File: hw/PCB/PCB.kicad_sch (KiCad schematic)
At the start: 283 parts, among them IC1 TXU0101DCKR, IC2 W25Q64JVXGIQ_TR, J1 USB_C_Receptacle_USB2.0, J2 Adafruit TFT, J3 Conn_ARM_JTAG_SWD_10, J4 Conn_01x03_Pin, K1 KEYSW, K10 KEYSW, K11 KEYSW, K12 KEYSW, K13 KEYSW, K14 KEYSW, K15 KEYSW, K16 KEYSW, K17 KEYSW, K18 KEYSW, K19 KEYSW, K2 KEYSW, K20 KEYSW, K21 KEYSW, K22 KEYSW, K23 KEYSW, K24 KEYSW, K25 KEYSW, K26 KEYSW, K27 KEYSW, K28 KEYSW, K29 KEYSW, K3 KEYSW, K31 KEYSW, K32 KEYSW, K33 KEYSW, K34 KEYSW, K35 KEYSW, K36 KEYSW, K37 KEYSW, K38 KEYSW, K39 KEYSW, K4 KEYSW, K40 KEYSW, K41 KEYSW, K42 KEYSW, K43 KEYSW, K46 KEYSW, K47 KEYSW, K48 KEYSW, K49 KEYSW, K5 KEYSW, K50 KEYSW, K51 KEYSW, K52 KEYSW, K53 KEYSW, K54 KEYSW, K55 KEYSW, K56 KEYSW, K57 KEYSW, K58 KEYSW, K59 KEYSW, K6 KEYSW, K61 KEYSW, K62 KEYSW, K63 KEYSW, K64 KEYSW, K65 KEYSW, K66 KEYSW, K67 KEYSW, K68 KEYSW, K69 KEYSW, K7 KEYSW, K8 KEYSW, K9 KEYSW, SW2 RotaryEncoder_Switch, U2 nRF52840-MS88SF2, U3 74HC595, U4 74HC595, U5 nPM1300-QEAA

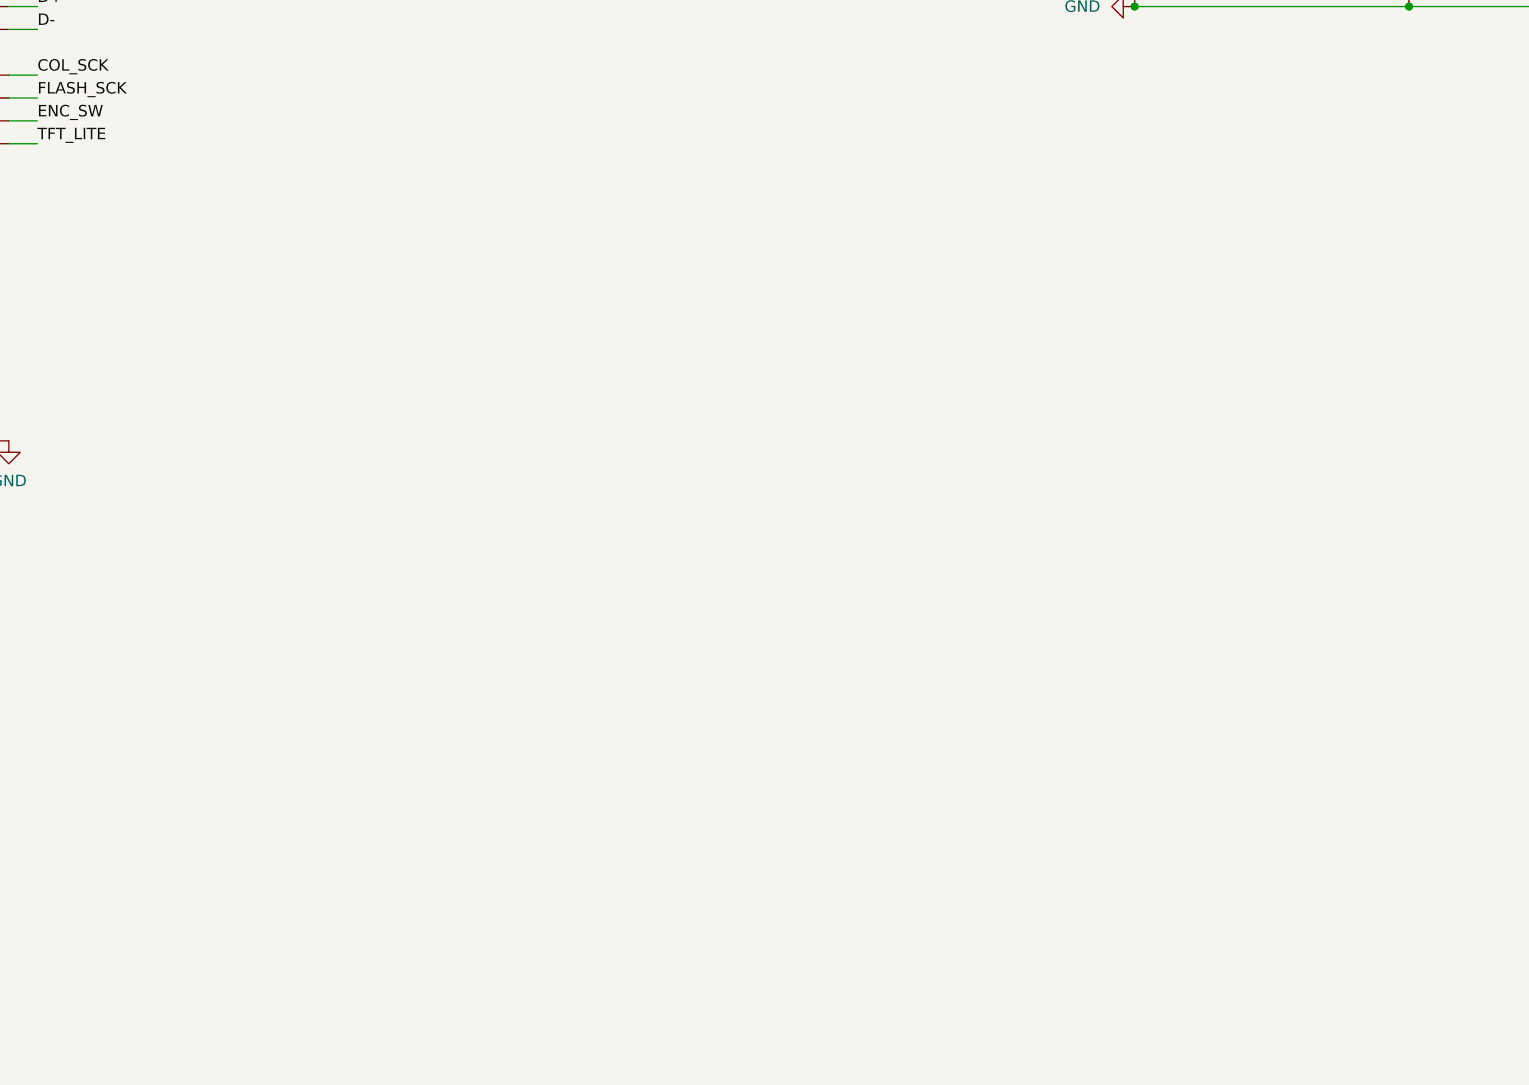
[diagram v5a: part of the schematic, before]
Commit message: Added XIAO and ItsyBitsy
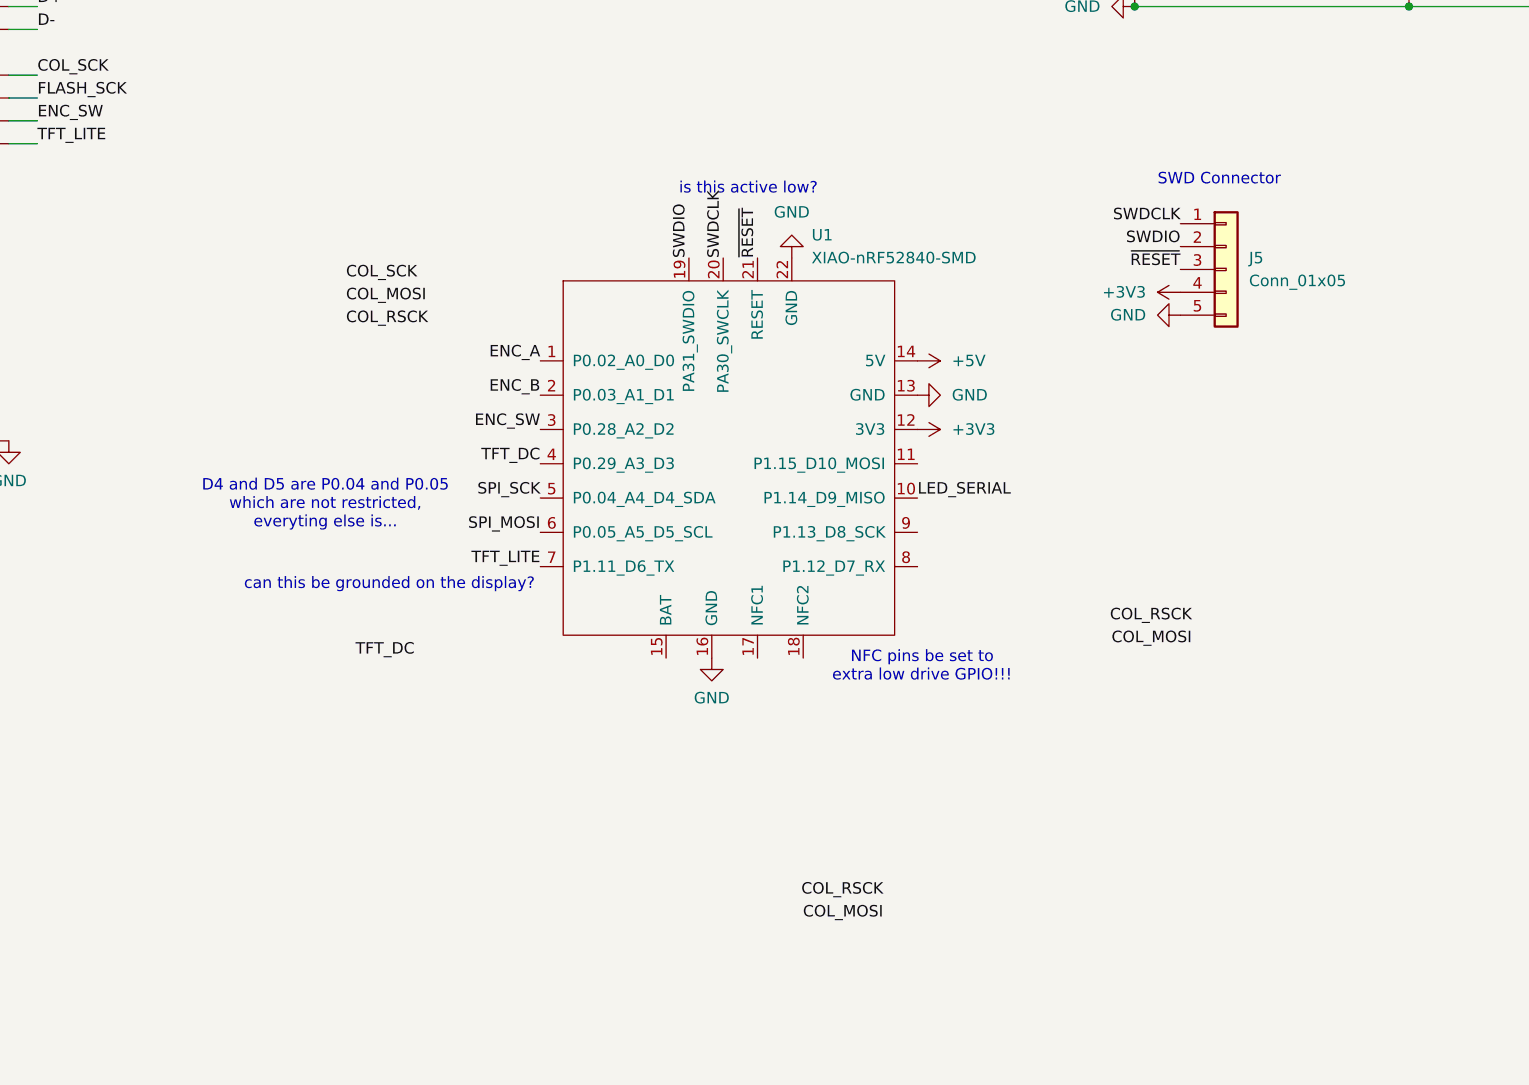
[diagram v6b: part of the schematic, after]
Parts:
- added J5: Conn_01x05, symbol Connector_Generic:Conn_01x05
- added U1: XIAO-nRF52840-SMD, Seeed Studio XIAO Series Library:XIAO-nRF52840-SMD, symbol Seeed_Studio_XIAO_Series:XIAO-nRF52840-SMD
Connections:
- net ENC_A: now also U1.1 (P0.02_A0_D0)
- net ENC_B: now also U1.2 (P0.03_A1_D1)
- net ENC_SW: now also U1.3 (P0.28_A2_D2)
- net GND: now also J5.5 (Pin_5), U1.13 (GND), U1.16 (GND), U1.22 (GND)
- net LED_SERIAL: now also U1.10 (P1.14_D9_MISO)
- net SWDCLK: now also J5.1 (Pin_1), U1.20 (PA30_SWCLK)
- net SWDIO: now also J5.2 (Pin_2), U1.19 (PA31_SWDIO)
- net TFT_DC: now also U1.4 (P0.29_A3_D3)
- net TFT_LITE: now also U1.7 (P1.11_D6_TX)
- net ~{RESET}: now also J5.3 (Pin_3), U1.21 (RESET)
- new net +3V3: J5.4 (Pin_4), U1.12 (3V3)
- new net +5V: U1.14 (5V)
- new net SPI_MOSI: U1.6 (P0.05_A5_D5_SCL)
- new net SPI_SCK: U1.5 (P0.04_A4_D4_SDA)
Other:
- note added: "D4 and D5 are P0.04 and P0.05 which are not restricted, everyting else is..."
- note added: "NFC pins be set to extra low drive GPIO!!!"
- note added: "SWD Connector"
- note added: "can this be grounded on the display?"
- note added: "is this active low?"

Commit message: beep boop more changes
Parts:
- removed BT1: ~, Connector_JST:JST_GH_SM03B-GHS-TB_1x03-1MP_P1.25mm_Horizontal, symbol PCB-altium-import:root_0_Battery_pack_NTC
- removed C11: 2.2uF, Capacitor_SMD:C_0603_1608Metric, symbol Device:C
- removed C12: 100nF, Capacitor_SMD:C_0201_0603Metric, symbol Device:C
- removed C13, C93: 1uF, Capacitor_SMD:C_0603_1608Metric, symbol Device:C
- removed C16: 10uF, Capacitor_SMD:C_0603_1608Metric, symbol Device:C
- removed C17: 100nF, Capacitor_SMD:C_0603_1608Metric, symbol Device:C
- removed D30: PRTR5V0U2X, Package_TO_SOT_SMD:SOT-143, symbol Power_Protection:PRTR5V0U2X
- removed IC2: W25Q64JVXGIQ_TR, W25Q64JVXGIQ_TR:SON80P400X400X50-9N, symbol W25Q64JVXGIQ_TR:W25Q64JVXGIQ_TR
- removed J1: USB_C_Receptacle_USB2.0, Adafruit-USB-C-Downstream-Breakout-master:Adafruit_USB_C_2.0, symbol Connector:USB_C_Receptacle_USB2.0
- removed J3: Conn_ARM_JTAG_SWD_10, Connector_PinHeader_1.27mm:PinHeader_2x05_P1.27mm_Vertical, symbol Connector:Conn_ARM_JTAG_SWD_10
- removed J4: Conn_01x03_Pin, Connector_PinHeader_2.54mm:PinHeader_1x03_P2.54mm_Vertical, symbol Connector:Conn_01x03_Pin
- removed R1, R2: 10K, Resistor_SMD:R_0603_1608Metric, symbol Device:R
- removed U2: nRF52840-MS88SF2, MS88SF2:XCVR_MS88SF2, symbol MS88SF2:MS88SF2
- removed U5: nPM1300-QEAA, nPM1300:nPM1300-QEAA, symbol PCB-altium-import:root_0_nPM1300_QEAA
- added J1: Conn_01x02, Connector_PinHeader_2.54mm:PinHeader_1x02_P2.54mm_Vertical, symbol Connector_Generic:Conn_01x02
- J5: footprint (none) -> Connector_PinHeader_2.54mm:PinHeader_1x05_P2.54mm_Vertical
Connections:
- net COL_RSCK is gone; now on net COL_CS: U3.12 (RCLK), U4.12 (RCLK)
- net TFT_MOSI is gone; now on net TFT_COL_MOSI: J2.6 (Pin_6)
- net TFT_SCK is gone; now on net TFT_COL_SCK: J2.4 (Pin_4)
- net VDD is gone; now on net +3V3: C14.2, IC1.1 (VCCA), J2.1 (Pin_1), U3.10 (~{SRCLR}), U3.16 (VCC), U4.10 (~{SRCLR}), U4.16 (VCC)
- net VSYS is gone; now on net +5V: C1.1, C10.1, C15.2, C19.1, C2.1, C20.1, C21.1, C22.1, C23.1, C24.1, C25.1, C26.1, C27.1, C28.1, C29.1, C3.1, C30.1, C31.1, C32.1, C33.1, C34.1, C35.1, C36.1, C37.1, C38.1, C39.1, C4.1, C40.1, C41.1, C42.1, C43.1, C44.1, C45.1, C46.1, C48.1, C49.1, C5.1, C50.1, C51.1, C52.1, C53.1, C54.1, C55.1, C56.1, C57.1, C58.1, C59.1, C6.1, C60.1, C61.1, C62.1, C63.1, C64.1, C65.1, C66.1, C67.1, C68.1, C69.1, C7.1, C70.1, C71.1, C72.1, C73.1, C74.1, C8.1, C9.1, IC1.5 (OE), IC1.6 (VCCB), LED1.1 (VDD), LED10.1 (VDD), LED11.1 (VDD), LED12.1 (VDD), LED13.1 (VDD), LED14.1 (VDD), LED15.1 (VDD), LED16.1 (VDD), LED17.1 (VDD), LED18.1 (VDD), LED19.1 (VDD), LED2.1 (VDD), LED20.1 (VDD), LED21.1 (VDD), LED22.1 (VDD), LED23.1 (VDD), LED24.1 (VDD), LED25.1 (VDD), LED26.1 (VDD), LED27.1 (VDD), LED28.1 (VDD), LED29.1 (VDD), LED3.1 (VDD), LED30.1 (VDD), LED31.1 (VDD), LED32.1 (VDD), LED33.1 (VDD), LED34.1 (VDD), LED35.1 (VDD), LED36.1 (VDD), LED37.1 (VDD), LED38.1 (VDD), LED39.1 (VDD), LED4.1 (VDD), LED40.1 (VDD), LED41.1 (VDD), LED42.1 (VDD), LED43.1 (VDD), LED46.1 (VDD), LED47.1 (VDD), LED48.1 (VDD), LED49.1 (VDD), LED5.1 (VDD), LED50.1 (VDD), LED51.1 (VDD), LED52.1 (VDD), LED53.1 (VDD), LED54.1 (VDD), LED55.1 (VDD), LED56.1 (VDD), LED57.1 (VDD), LED58.1 (VDD), LED59.1 (VDD), LED6.1 (VDD), LED61.1 (VDD), LED62.1 (VDD), LED63.1 (VDD), LED64.1 (VDD), LED65.1 (VDD), LED66.1 (VDD), LED67.1 (VDD), LED68.1 (VDD), LED7.1 (VDD), LED8.1 (VDD), LED9.1 (VDD)
- net ENC_A: now also U1.11 (P1.15_D10_MOSI); no longer U1.1 (P0.02_A0_D0)
- net ENC_B: now also U1.10 (P1.14_D9_MISO); no longer U1.2 (P0.03_A1_D1)
- net GND: now also J1.2 (Pin_2); no longer J2.7 (Pin_7)
- net LED_SERIAL: now also U1.1 (P0.02_A0_D0); no longer U1.10 (P1.14_D9_MISO)
- net ROW0: now also U1.3 (P0.28_A2_D2)
- net ROW1: now also U1.2 (P0.03_A1_D1)
- net ROW2: now also U1.7 (P1.11_D6_TX)
- net SWDCLK: now also J5.2 (Pin_2); no longer J5.1 (Pin_1)
- net SWDIO: now also J5.1 (Pin_1); no longer J5.2 (Pin_2)
- net TFT_DC: now also U1.17 (NFC1); no longer U1.4 (P0.29_A3_D3)
- net TFT_LITE: no longer U1.7 (P1.11_D6_TX)
- net VBAT: now also U1.15 (BAT), J1.1 (Pin_1)
- net TFT_CS: now reaches U1.18 (NFC2)
- net TFT_CS: now also J2.7 (Pin_7)
- net COL_CS: now reaches U1.9 (P1.13_D8_SCK)
- net ENC_SW: no longer names the net of SW2.S2
- net ENC_SW: no longer U1.3 (P0.28_A2_D2)
- net SPI_MOSI renamed TFT_COL_MOSI
- net SPI_SCK renamed TFT_COL_SCK
- net ~{RESET} renamed RESET
- no-connect marks 19 -> 9
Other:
- note added: "NFC pins can be set to extra low drive GPIO!!!"
- note added: "TFT and shift registers can be on the same bus while nothing else can be on the LED bus"
- note added: "Tradeoffs: TFT and shift register SPI have been combined No encoder switch No TFT backlight dimming"
- note added: "need to route the other way :)"
- note removed: "0Ω 0.0 V 4.7 kΩ 1.0 V 10 kΩ 1.2 V 22 kΩ 1.5 V 47 kΩ 1.8 V 68 kΩ 2.0 V 100 kΩ 2.2 V 150 kΩ 2.5 V 250-500 kΩ 2.7 V"
- note removed: "0Ω 0.0 V 4.7 kΩ 1.8 V 10 kΩ 2.0 V 22 kΩ 2.2 V 47 kΩ 2.4 V 68 kΩ 2.5 V 100 kΩ 2.7 V 150 kΩ 3.0 V 250-500 kΩ 3.3 V"
- note removed: "Board should be powered through USB or battery for flash/debug"
- note removed: "NFC pins be set to extra low drive GPIO!!!"
- note removed: "Pull-ups not needed MCU internals are low enough (13k)"
- note removed: "This is for VBUS sensing only, cannot be loaded"
- note removed: "Unregulated 5V or 3.7V (USB vs LiPo)"
- note removed: "VSET1"
- note removed: "VSET2"
- note removed: "can this be grounded on the display?"
- note removed: "is this active low?"
- note removed: "nRF52840"
- note removed: "to bypass npm1300 if needed"
- moved on the sheet: J5, SW2, U1

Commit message: routing
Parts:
- removed C14, C15: 100nF, Capacitor_SMD:C_0603_1608Metric, symbol Device:C
- added C11, C12: 100nF, Capacitor_SMD:C_0603_1608Metric, symbol Device:C
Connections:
- net +3V3: now also C11.2
- net +5V: now also C12.2
- net GND: now also C11.1, C12.1
- net ROW0: now also U1.2 (P0.03_A1_D1); no longer U1.3 (P0.28_A2_D2)
- net ROW1: now also U1.3 (P0.28_A2_D2); no longer U1.2 (P0.03_A1_D1)
- net at LED34.2 (DOUT): now also LED33.4 (DIN); no longer LED35.4 (DIN)
- net at LED34.4 (DIN): now also LED35.2 (DOUT); no longer LED33.2 (DOUT)
- net at LED66.2 (DOUT): now also LED65.4 (DIN); no longer LED67.4 (DIN)
- net at LED66.4 (DIN): now also LED67.2 (DOUT); no longer LED65.2 (DOUT)
- net at LED10.2 (DOUT): now also LED9.4 (DIN); no longer LED11.4 (DIN)
- net at LED10.4 (DIN): now also LED11.2 (DOUT); no longer LED9.2 (DOUT)
- net at LED47.2 (DOUT): now also LED48.4 (DIN); no longer LED46.4 (DIN)
- net at LED47.4 (DIN): now also LED46.2 (DOUT); no longer LED48.2 (DOUT)
- net at LED17.2 (DOUT): now also LED18.4 (DIN); no longer LED16.4 (DIN)
- net at LED17.4 (DIN): now also LED16.2 (DOUT); no longer LED18.2 (DOUT)
- net at LED5.2 (DOUT): now also LED4.4 (DIN); no longer LED6.4 (DIN)
- net at LED5.4 (DIN): now also LED6.2 (DOUT); no longer LED4.2 (DOUT)
- net at LED37.2 (DOUT): now also LED36.4 (DIN); no longer LED38.4 (DIN)
- net at LED37.4 (DIN): now also LED38.2 (DOUT); no longer LED36.2 (DOUT)
- net at LED63.2 (DOUT): now also LED62.4 (DIN); no longer LED64.4 (DIN)
- net at LED63.4 (DIN): now also LED64.2 (DOUT); no longer LED62.2 (DOUT)
- net at LED41.2 (DOUT): now also LED40.4 (DIN); no longer LED42.4 (DIN)
- net at LED41.4 (DIN): now also LED42.2 (DOUT); no longer LED40.2 (DOUT)
- net at LED31.2 (DOUT): now also LED46.4 (DIN); no longer LED32.4 (DIN)
- net at LED31.4 (DIN): now also LED32.2 (DOUT); no longer LED46.2 (DOUT)
- net at LED1.4 (DIN): now also LED2.2 (DOUT); no longer LED16.2 (DOUT)
- net at LED55.2 (DOUT): now also LED56.4 (DIN); no longer LED54.4 (DIN)
- net at LED55.4 (DIN): now also LED54.2 (DOUT); no longer LED56.2 (DOUT)
- net at LED59.2 (DOUT): now also LED30.4 (DIN); no longer LED58.4 (DIN)
- net at LED59.4 (DIN): now also LED58.2 (DOUT); no longer LED30.2 (DOUT)
- net at LED19.2 (DOUT): now also LED20.4 (DIN); no longer LED18.4 (DIN)
- net at LED19.4 (DIN): now also LED18.2 (DOUT); no longer LED20.2 (DOUT)
- net at LED61.4 (DIN): now also LED62.2 (DOUT); no longer IC1.4 (BY)
- net at LED21.2 (DOUT): now also LED22.4 (DIN); no longer LED20.4 (DIN)
- net at LED21.4 (DIN): now also LED20.2 (DOUT); no longer LED22.2 (DOUT)
- net at LED39.2 (DOUT): now also LED38.4 (DIN); no longer LED40.4 (DIN)
- net at LED39.4 (DIN): now also LED40.2 (DOUT); no longer LED38.2 (DOUT)
- net at LED28.2 (DOUT): now also LED29.4 (DIN); no longer LED27.4 (DIN)
- net at LED28.4 (DIN): now also LED27.2 (DOUT); no longer LED29.2 (DOUT)
- net at LED3.2 (DOUT): now also LED2.4 (DIN); no longer LED4.4 (DIN)
- net at LED3.4 (DIN): now also LED4.2 (DOUT); no longer LED2.2 (DOUT)
- net at LED15.2 (DOUT): now also LED68.4 (DIN); no longer LED30.4 (DIN)
- net at LED1.2 (DOUT): now also LED16.4 (DIN); no longer LED2.4 (DIN)
- net at LED43.4 (DIN): now also LED29.2 (DOUT); no longer LED42.2 (DOUT)
- net at LED15.4 (DIN): now also LED30.2 (DOUT); no longer LED68.2 (DOUT)
- net at LED23.2 (DOUT): now also LED24.4 (DIN); no longer LED22.4 (DIN)
- net at LED23.4 (DIN): now also LED22.2 (DOUT); no longer LED24.2 (DOUT)
- net at LED8.2 (DOUT): now also LED7.4 (DIN); no longer LED9.4 (DIN)
- net at LED8.4 (DIN): now also LED9.2 (DOUT); no longer LED7.2 (DOUT)
- net at LED61.2 (DOUT): no longer LED62.4 (DIN)
- net at LED12.2 (DOUT): now also LED11.4 (DIN); no longer LED13.4 (DIN)
- net at LED12.4 (DIN): now also LED13.2 (DOUT); no longer LED11.2 (DOUT)
- net at LED49.2 (DOUT): now also LED50.4 (DIN); no longer LED48.4 (DIN)
- net at LED26.4 (DIN): now also LED25.2 (DOUT); no longer LED27.2 (DOUT)
- net at LED57.2 (DOUT): now also LED58.4 (DIN); no longer LED56.4 (DIN)
- net at LED51.2 (DOUT): now also LED52.4 (DIN); no longer LED50.4 (DIN)
- net at LED51.4 (DIN): now also LED50.2 (DOUT); no longer LED52.2 (DOUT)
- net at LED43.2 (DOUT): now also LED42.4 (DIN); no longer LED29.4 (DIN)
- net at LED14.4 (DIN): now also IC1.4 (BY); no longer LED13.2 (DOUT)
- net at LED57.4 (DIN): now also LED56.2 (DOUT); no longer LED58.2 (DOUT)
- net at LED53.4 (DIN): now also LED52.2 (DOUT); no longer LED54.2 (DOUT)
- net at LED49.4 (DIN): now also LED48.2 (DOUT); no longer LED50.2 (DOUT)
- net at LED14.2 (DOUT): now also LED13.4 (DIN)
- net at LED53.2 (DOUT): now also LED54.4 (DIN); no longer LED52.4 (DIN)
- net at LED26.2 (DOUT): now also LED27.4 (DIN); no longer LED25.4 (DIN)
- new net: LED32.4 (DIN), LED33.2 (DOUT)
- new net: LED35.4 (DIN), LED36.2 (DOUT)
- new net: LED6.4 (DIN), LED7.2 (DOUT)
- new net: LED67.4 (DIN), LED68.2 (DOUT)
- new net: LED64.4 (DIN), LED65.2 (DOUT)
- new net: LED24.2 (DOUT), LED25.4 (DIN)
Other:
- note added: "Level Shifter for 3.3V->5V"
- note removed: "Level shifter for VDD->VSYS translation"
